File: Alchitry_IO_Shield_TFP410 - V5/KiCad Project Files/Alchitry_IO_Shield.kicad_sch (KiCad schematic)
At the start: 1 part, among them U1 Alchitry_Single

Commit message: laid out switches, btns and leds
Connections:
- net B0: no longer U1.C_20 (N4)
- net B1: no longer U1.C_21 (M5)
- net B2: no longer U1.C_23 (L5)
- net B3: no longer U1.C_24 (P5)
- net CLK: no longer U1.C_43 (P13)
- net DE: no longer U1.C_42 (N13)
- net DIP0: no longer U1.B_30 (D6)
- net DIP1: now also U1.C_27 (T4); no longer U1.B_31 (D5)
- net DIP10: now also U1.C_40 (M1); no longer U1.B_45 (C3)
- net DIP11: now also U1.C_42 (N13); no longer U1.B_46 (C2)
- net DIP12: now also U1.C_43 (P13); no longer U1.B_48 (C1)
- net DIP13: now also U1.C_45 (N11); no longer U1.B_49 (B1)
- net DIP14: now also U1.C_46 (N12); no longer U1.A_27 (M6)
- net DIP15: now also U1.C_48 (P10); no longer U1.A_28 (N6)
- net DIP2: now also U1.C_28 (T3); no longer U1.B_33 (F5)
- net DIP3: now also U1.C_30 (R3); no longer U1.B_34 (E5)
- net DIP4: now also U1.C_31 (T2); no longer U1.B_36 (G5)
- net DIP5: now also U1.C_33 (R2); no longer U1.B_37 (G4)
- net DIP6: now also U1.C_34 (R1); no longer U1.B_39 (D4)
- net DIP7: now also U1.C_36 (N1); no longer U1.B_40 (C4)
- net DIP8: now also U1.C_37 (P1); no longer U1.B_42 (E3)
- net DIP9: now also U1.C_39 (M2); no longer U1.B_43 (D3)
- net G0: no longer U1.C_31 (T2)
- net G1: no longer U1.C_30 (R3)
- net G2: no longer U1.C_28 (T3)
- net G3: no longer U1.C_27 (T4)
- net HS: no longer U1.C_39 (M2)
- net LED1: now also U1.A_27 (M6); no longer U1.B_20 (B5)
- net LED10: now also U1.A_40 (K2); no longer U1.A_42 (N9)
- net LED11: now also U1.A_42 (N9); no longer U1.A_43 (P9)
- net LED12: now also U1.A_43 (P9); no longer U1.A_45 (R7)
- net LED13: now also U1.A_45 (R7); no longer U1.A_46 (R6)
- net LED14: now also U1.A_46 (R6); no longer U1.A_48 (T9)
- net LED15: now also U1.A_48 (T9); no longer U1.A_49 (T10)
- net LED2: now also U1.A_28 (N6); no longer U1.B_18 (A5)
- net LED3: now also U1.A_30 (H5); no longer U1.B_17 (A4)
- net LED4: now also U1.A_31 (H4); no longer U1.B_15 (B4)
- net LED5: now also U1.A_33 (J3); no longer U1.B_14 (A3)
- net LED6: now also U1.A_34 (H3); no longer U1.B_12 (F4)
- net LED7: now also U1.A_36 (J5); no longer U1.B_11 (F3)
- net LED8: now also U1.A_37 (J4); no longer U1.A_39 (K3)
- net LED9: now also U1.A_39 (K3); no longer U1.A_40 (K2)
- net R0: no longer U1.C_37 (P1)
- net R1: no longer U1.C_36 (N1)
- net R2: no longer U1.C_34 (R1)
- net R3: no longer U1.C_33 (R2)
- net SWL1: no longer U1.B_28 (C6)
- net SWL2: no longer U1.B_27 (C7)
- net SWL3: no longer U1.B_23 (A7)
- net SWL4: no longer U1.B_24 (B7)
- net SWR1: now also U1.B_5 (A2); no longer U1.C_46 (N12)
- net SWR2: now also U1.B_2 (D1); no longer U1.C_49 (P11)
- net SWR3: now also U1.B_3 (E2); no longer U1.C_48 (P10)
- net SWR4: now also U1.B_6 (B2); no longer U1.C_45 (N11)
- net VS: no longer U1.C_40 (M1)
- net CR3: now reaches U1.B_8 (E1)
- net CR4: now reaches U1.B_9 (F2)
- net LED0 renamed ANR2
- new net ANR1: U1.B_20 (B5)
- new net ANR3: U1.B_23 (A7)
- new net ANR4: U1.B_24 (B7)
- new net CR1: U1.B_15 (B4)
- new net CR2: U1.B_11 (F3)
- new net CR5: U1.B_14 (A3)
- new net CR6: U1.B_17 (A4)
- new net CR7: U1.B_12 (F4)
- new net DIP16: U1.C_49 (P11)
- new net LED16: U1.A_49 (T10)
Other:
- sheet LEDs ports: added DIP[1..16], LED[1..16]; removed C[0..6], DIP[0..15], LED[0..15]

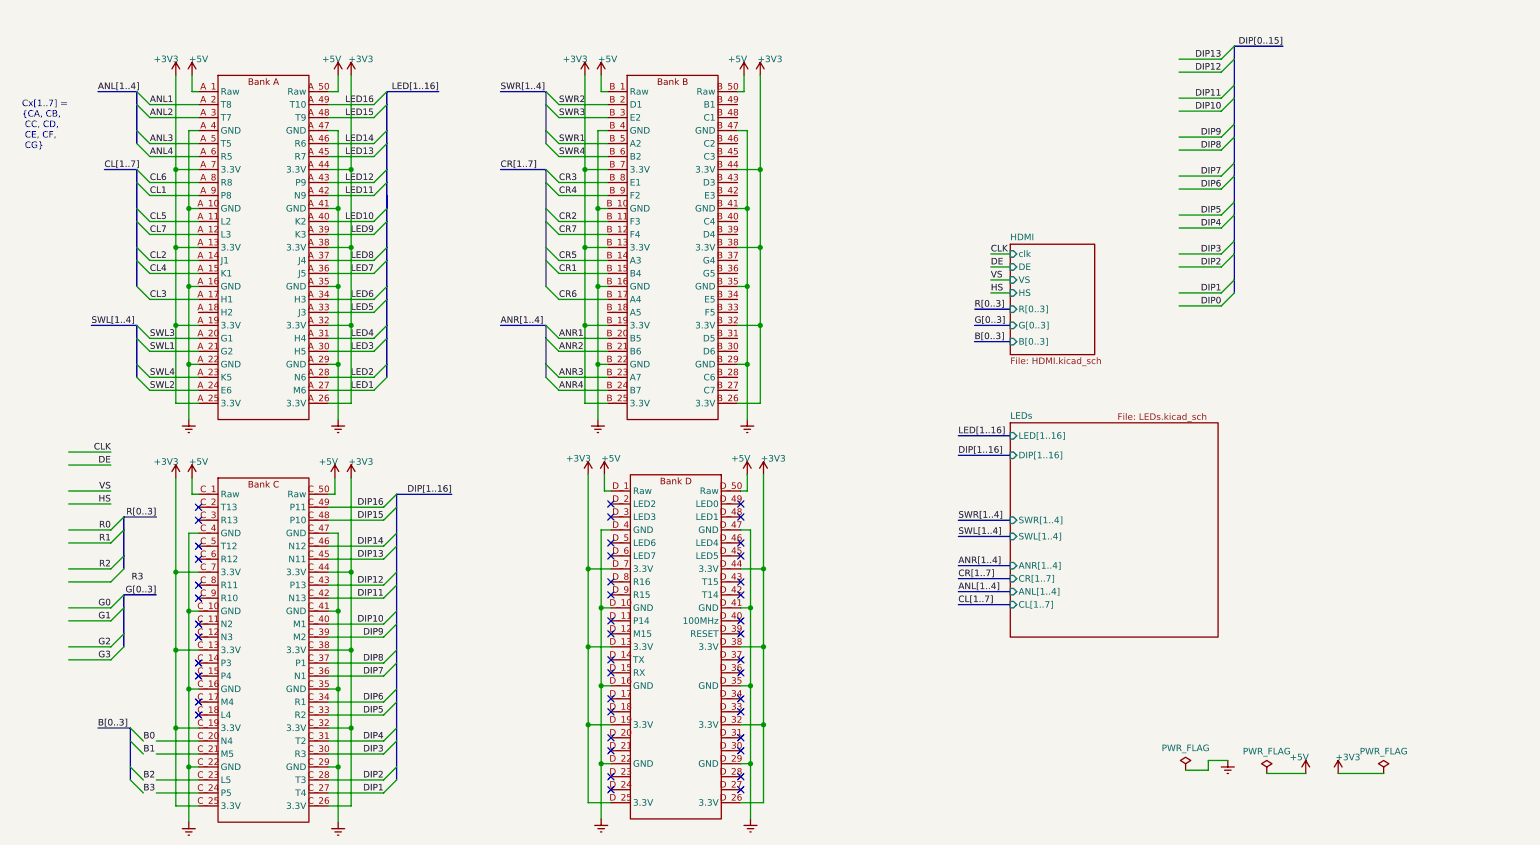
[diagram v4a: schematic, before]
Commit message: adding USB C for OTG programming and serial
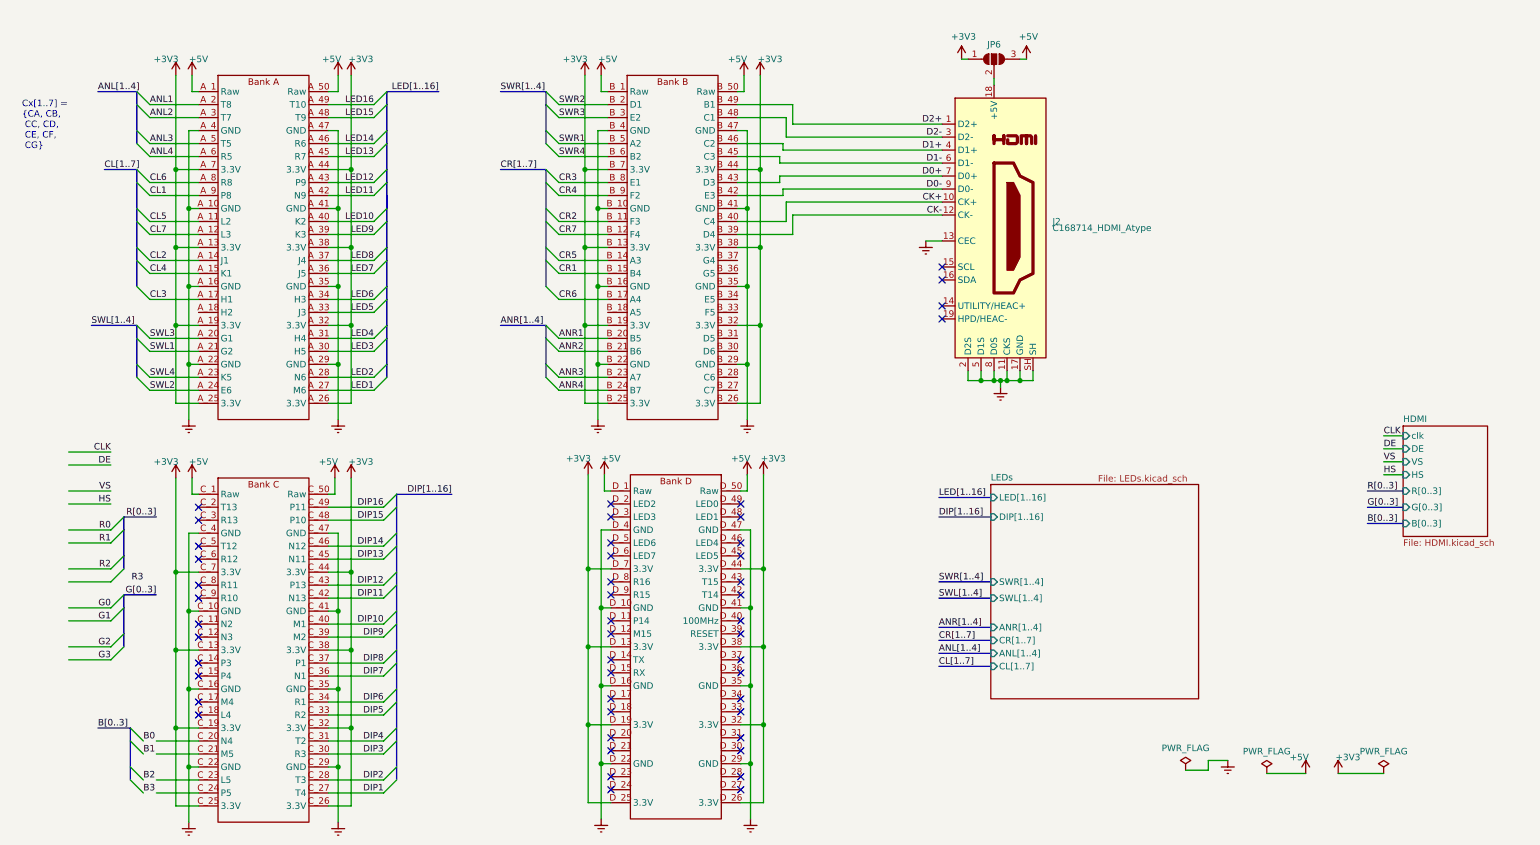
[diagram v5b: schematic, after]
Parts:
- added J2: C168714_HDMI_Atype, Custom_Connectors:C168714_HDMI_Atype, symbol Custom_Connectors:C168714_HDMI_Atype
- added JP6: V_Sel, Custom_Parts:jumper_unbridged, symbol Jumper:SolderJumper_3_Open
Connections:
- net +3V3: now also JP6.1 (A)
- net +5V: now also JP6.3 (B)
- net GNDREF: now also J2.11 (CKS), J2.13 (CEC), J2.17 (GND), J2.2 (D2S), J2.5 (D1S), J2.8 (D0S), J2.SH
- net CK-: now reaches U1.B_39 (D4)
- net CK-: now also J2.12 (CK-)
- net CK+: now reaches U1.B_40 (C4)
- net CK+: now also J2.10 (CK+)
- net D0-: now reaches U1.B_42 (E3)
- net D0-: now also J2.9 (D0-)
- net D0+: now reaches U1.B_43 (D3)
- net D0+: now also J2.7 (D0+)
- net D1-: now reaches U1.B_45 (C3)
- net D1-: now also J2.6 (D1-)
- net D1+: now reaches U1.B_46 (C2)
- net D1+: now also J2.4 (D1+)
- net D2-: now reaches U1.B_48 (C1)
- net D2-: now also J2.3 (D2-)
- net D2+: now reaches U1.B_49 (B1)
- net D2+: now also J2.1 (D2+)
- new net: J2.18 (+5V), JP6.2 (C)
- no-connect marks 44 -> 48

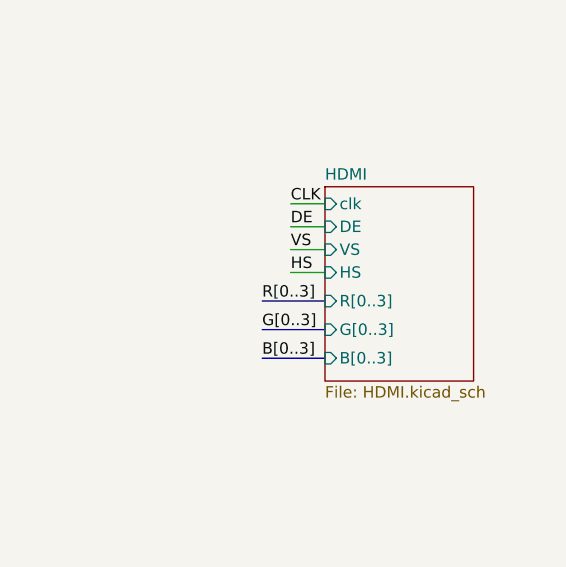
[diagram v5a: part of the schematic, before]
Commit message: updated shield v4 schematic
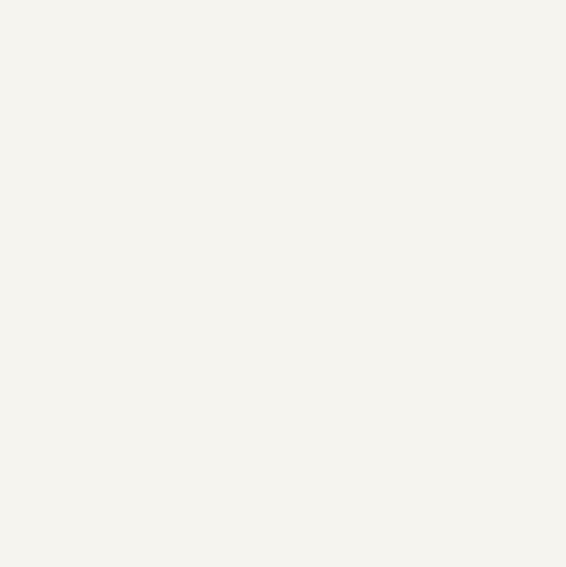
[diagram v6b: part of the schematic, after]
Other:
- removed sheet HDMI
